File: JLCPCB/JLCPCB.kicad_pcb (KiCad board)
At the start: 4 copper layers, 180 x 235 mm, 27 parts

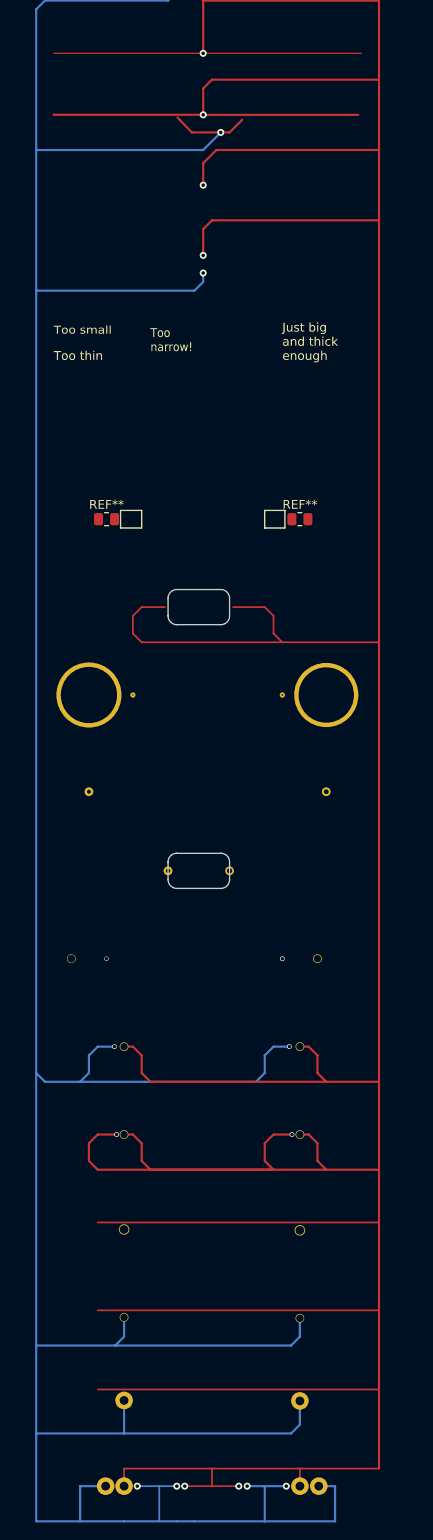
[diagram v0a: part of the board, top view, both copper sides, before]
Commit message: Refactor rules.
Add “Avoid 4-Wire Kelvin Test” rule.
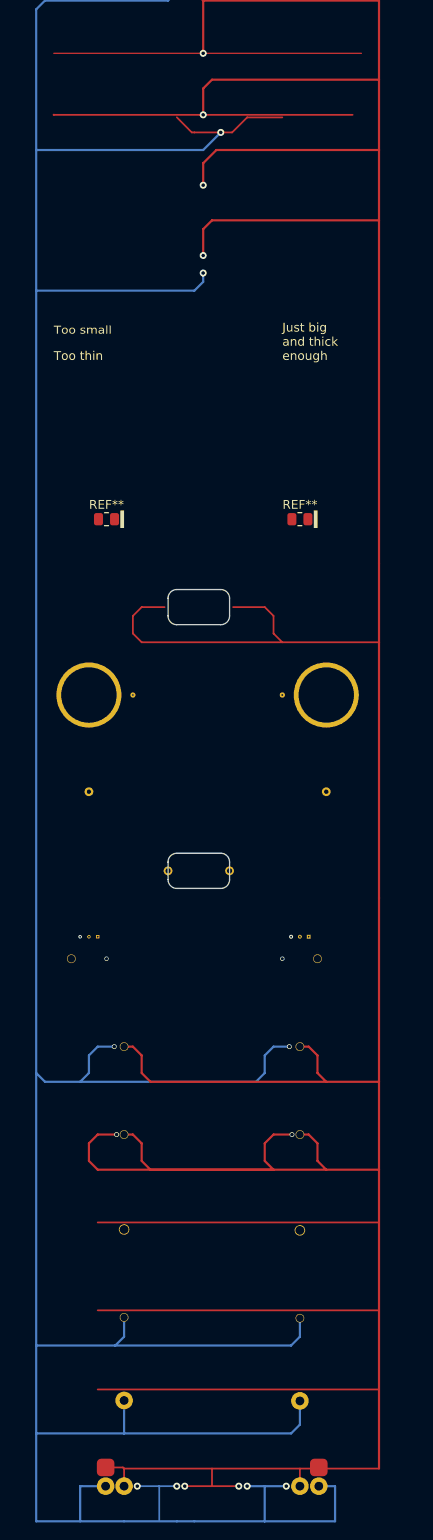
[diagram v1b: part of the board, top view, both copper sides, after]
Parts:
- added ?: , , F.Cu at (143.9, 126.6)
- added ?: , , F.Cu at (143.0, 126.6)
- added ?: , , F.Cu at (121.0, 187.0)
- added ?: , , F.Cu at (145.1, 187.0)
- added ?: , , F.Cu at (119.0, 126.5)
- added ?: , , F.Cu at (120.0, 126.5)
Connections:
- REF** pad 1: GND -> (no net) (x2)
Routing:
- net +5V: track 424.8 -> 429.2 mm
- net GND: track 694.5 -> 696.4 mm, vias 10 -> 8
- net (no net): vias 0 -> 4
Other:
- board text removed: "Too narrow!"
